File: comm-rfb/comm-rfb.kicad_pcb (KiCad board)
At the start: 4 copper layers, 90.2 x 95.9 mm, 59 parts, among them J1 PC104_Connector, J10 Radio Test Connector, J11 System Test Connector, J12 Programming Header, J2 TFM-110-02-SM-D-A-K-TR, J3 TFM-110-02-SM-D-A-K-TR, J4 TFM-110-02-SM-D-A-K-TR, J5 TFM-110-02-SM-D-A-K-TR, J6 Conn_Coaxial, J7 Conn_Coaxial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

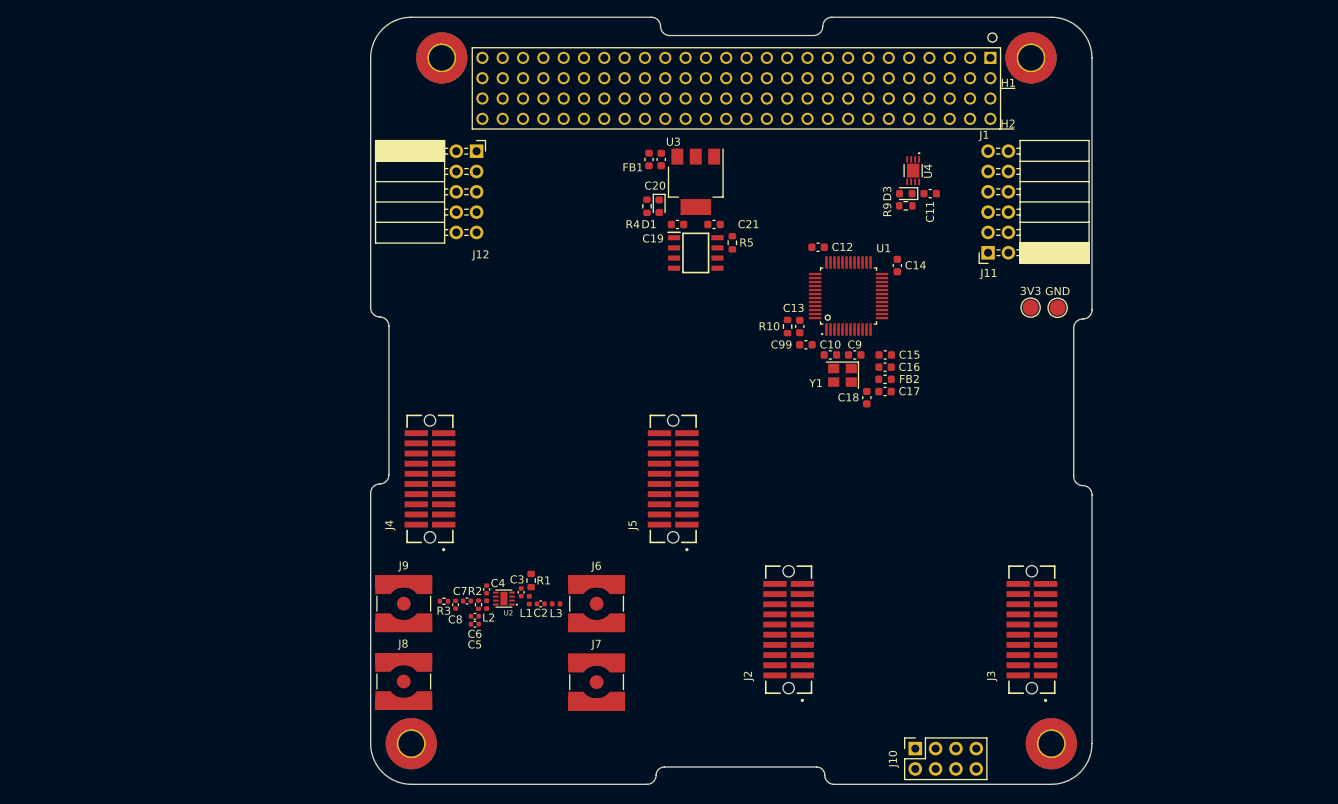
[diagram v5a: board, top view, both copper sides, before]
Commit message: comm-rfb: continue with new layout
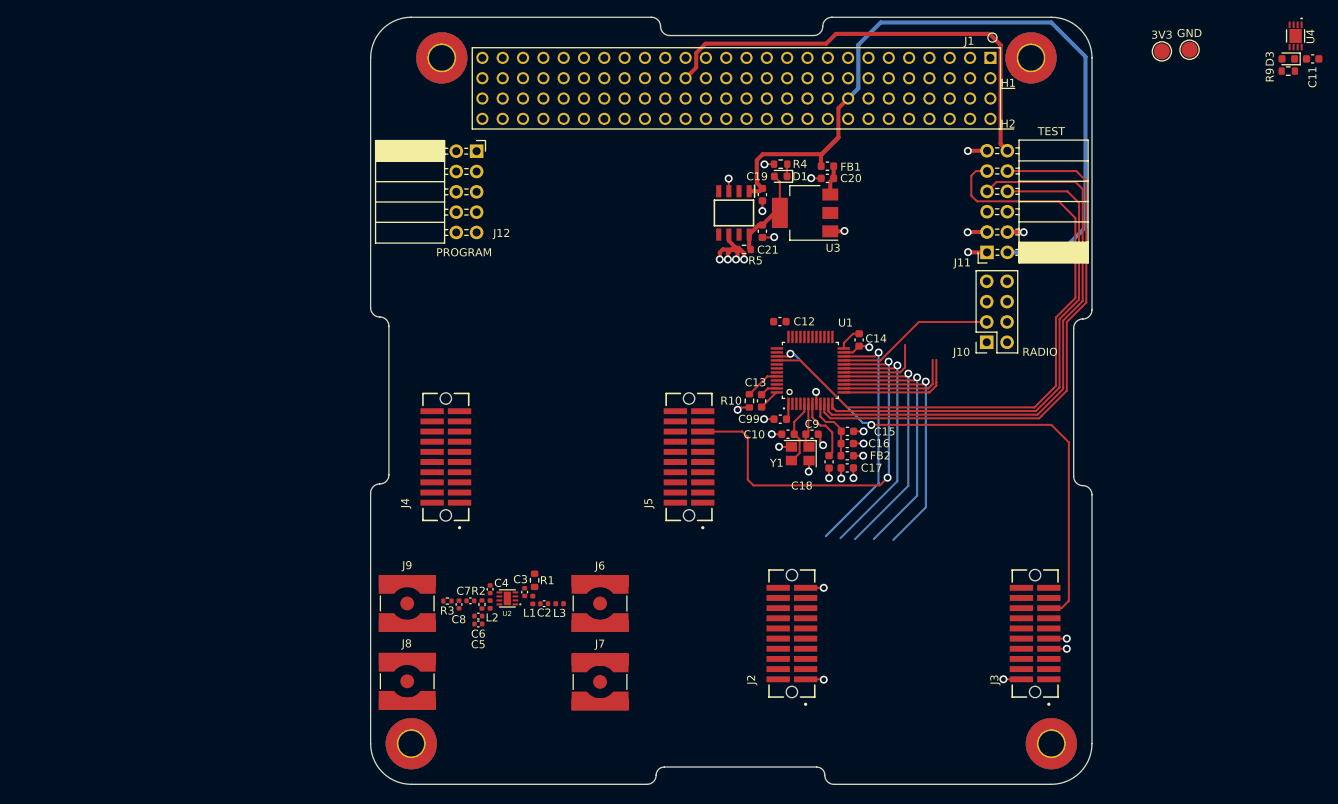
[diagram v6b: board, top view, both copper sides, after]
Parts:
- moved J10 51.6 mm to (186.2, 87.6), turned to 180 degrees
- moved C11 50.7 mm to (227.0, 52.2)
- moved D3 50.7 mm to (223.9, 52.2)
- moved R9 50.7 mm to (223.9, 53.7)
- moved U4 50.7 mm to (224.8, 49.3)
- moved TP2 36.2 mm to (211.6, 51.1)
- moved TP1 36.0 mm to (208.1, 51.3)
- moved FB1 22.3 mm to (166.3, 65.6), turned to 180 degrees
- moved C20 20.9 mm to (166.3, 67.1), turned to 180 degrees
- moved R4 17.5 mm to (160.5, 65.4), turned to 0 degrees
- moved D1 15.6 mm to (160.5, 66.9), turned to 180 degrees
- moved U3 14.2 mm to (163.5, 71.5), turned to 180 degrees
- moved C9 11.3 mm to (164.4, 99.1)
- moved C19 11.3 mm to (158.2, 69.2), turned to -90 degrees
- moved C10 11.2 mm to (161.4, 99.1)
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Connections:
- J1 pad 41: unconnected-(J1-Pad41) -> I2C2-SDA
- J1 pad 43: unconnected-(J1-Pad43) -> I2C2-SCK
- J11 pad 10: SYS-GPIO3 -> SYS-GPIO1
- J11 pad 5: I2C-SCK -> I2C2-SCK
- J11 pad 6: I2C-SDA -> I2C2-SDA
- J11 pad 8: SYS-GPIO1 -> SYS-GPIO3
- U1 pad 32: I2C2-SCLK -> I2C2-SCK
- U1 pad 45: I2C-SCK -> I2C1-SCK
- U1 pad 46: I2C-SDA -> I2C1-SDA
- U4 pad 2: I2C2-SCLK -> I2C2-SCK
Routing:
- net SW6-5V: track 0.00 -> 97.8 mm
- net SYS-GPIO4: track 0.00 -> 79.3 mm
- net SYS-GPIO1: track 0.00 -> 70.7 mm
- net SYS-GPIO2: track 0.00 -> 70.6 mm
- net RESET-RX: track 0.00 -> 63.9 mm, vias 0 -> 2
- net SYS-GPIO3: track 0.00 -> 63.9 mm
- net 5V0-CHG: track 0.00 -> 56.9 mm
- net RESET-TX: track 0.00 -> 49.7 mm, vias 0 -> 2
- net GND: track 0.36 -> 41.2 mm, vias 0 -> 23
- net SPI1-SCLK: track 0.00 -> 31.9 mm, vias 0 -> 1
- net SPI1-MISO: track 0.00 -> 31.8 mm, vias 0 -> 1
- net SPI1-MOSI: track 0.00 -> 31.6 mm, vias 0 -> 1
- net SPI1-CSN-RX: track 0.00 -> 31.4 mm, vias 0 -> 1
- net AMP-ENABLE: track 0.00 -> 30.3 mm, vias 0 -> 1
- net +3V3: track 0.00 -> 28.0 mm, vias 0 -> 9
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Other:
- board text added: "PROGRAM"
- board text added: "RADIO"
- board text added: "TEST"

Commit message: comm-rfb: finish connections from MCU
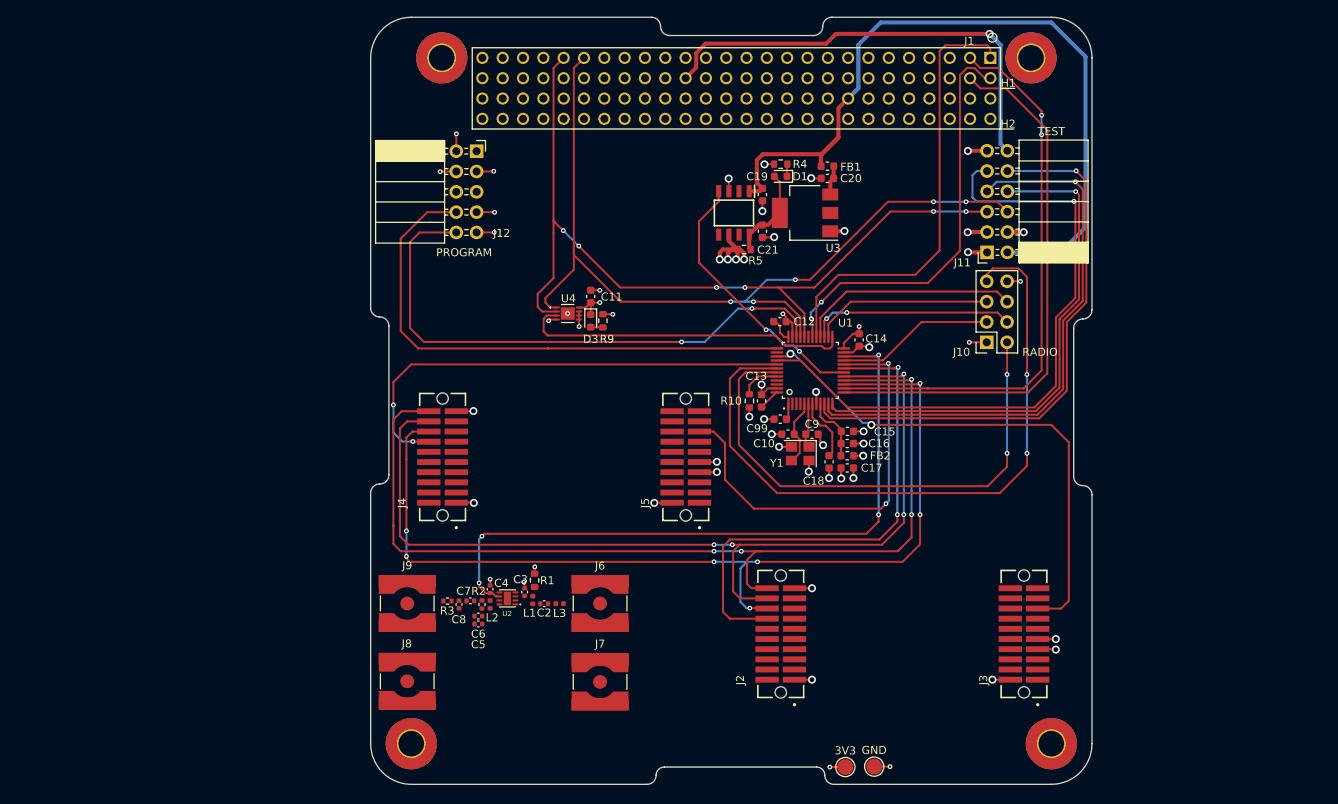
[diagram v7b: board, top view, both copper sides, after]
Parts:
- moved TP2 97.9 mm to (172.2, 140.7)
- moved TP1 97.8 mm to (168.6, 140.7)
- moved U4 97.4 mm to (133.9, 84.0), turned to 0 degrees
- moved C11 95.0 mm to (136.7, 81.9), turned to 90 degrees
- moved D3 93.1 mm to (136.7, 84.9), turned to -90 degrees
- moved R9 91.2 mm to (138.3, 84.9), turned to 90 degrees
- moved J2 1.39 mm to (160.5, 124.1)
- moved J3 1.39 mm to (190.9, 124.1)
- moved J5 0.41 mm to (148.6, 102.0)
- moved J4 0.41 mm to (118.2, 102.0)
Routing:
- net I2C2-SDA: track 0.00 -> 108.0 mm, vias 0 -> 5
- net I2C2-SCK: track 0.00 -> 104.2 mm, vias 0 -> 6
- net SPI1-MISO: track 31.8 -> 123.1 mm, vias 1 -> 4
- net SPI1-SCLK: track 31.9 -> 122.1 mm, vias 1 -> 7
- net SPI1-MOSI: track 31.6 -> 119.0 mm, vias 1 -> 4
- net SPI2-CSN: track 0.00 -> 86.1 mm, vias 0 -> 2
- net SWDIO: track 0.00 -> 70.5 mm, vias 0 -> 2
- net SWCLK: track 0.00 -> 67.8 mm
- net SPI2-CE: track 0.00 -> 65.6 mm, vias 0 -> 2
- net SPI1-CSN-TX: track 0.00 -> 60.1 mm, vias 0 -> 2
- net COMM-TXD: track 0.00 -> 55.7 mm
- net COMM-CTS: track 14.4 -> 69.8 mm, vias 0 -> 2
- net AMP-ENABLE: track 30.3 -> 85.1 mm, vias 1 -> 4
- net COMM-RTS: track 15.1 -> 69.2 mm
- net COMM-RXD: track 0.00 -> 51.6 mm, vias 0 -> 2
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
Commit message: comm-rfb: finish RF front end
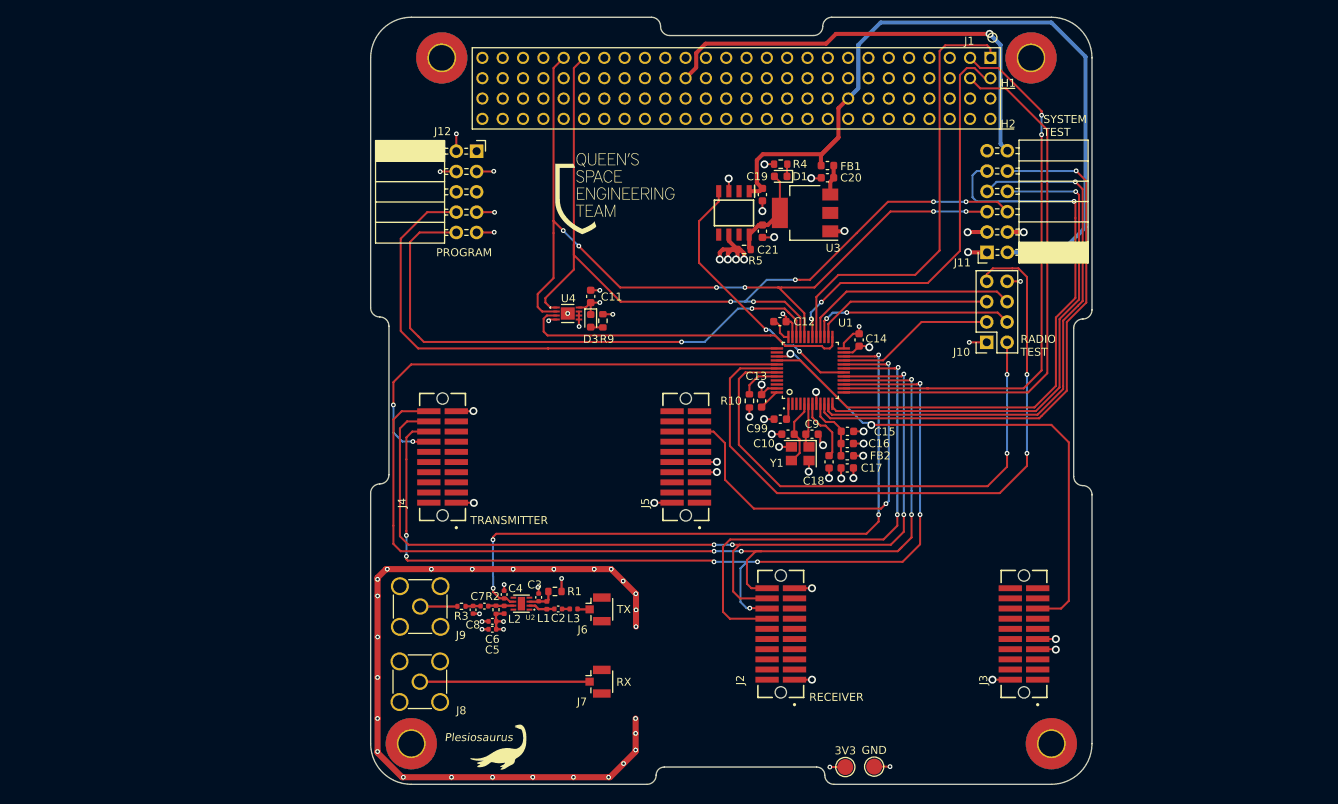
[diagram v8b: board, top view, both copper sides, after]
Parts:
- added G***: LOGO, LOGO, F.Cu at (139.8, 68.9)
- added G***: LOGO, LOGO, F.Cu at (125.2, 138.2)
- J6, J7: footprint Connector_Coaxial:SMA_Amphenol_132134-10_Vertical -> Connector_Coaxial:U.FL_Hirose_U.FL-R-SMT-1_Vertical
- J8, J9: footprint Connector_Coaxial:SMA_Amphenol_132134-10_Vertical -> Connector_Coaxial:SMA_Amphenol_132134-11_Vertical
- moved R1 2.90 mm to (132.3, 118.8), turned to 180 degrees
- moved L1 1.87 mm to (131.2, 120.5)
- moved L3 1.87 mm to (134.6, 121.0)
- moved C8 1.87 mm to (122.0, 121.1)
- moved R3 1.87 mm to (120.6, 120.6)
- moved C4 1.87 mm to (125.9, 119.2)
- moved C5 1.87 mm to (124.4, 123.5)
- moved C6 1.87 mm to (124.4, 122.5)
- moved C7 1.87 mm to (123.4, 120.6)
- moved L2 1.87 mm to (125.9, 121.1)
- moved R2 1.87 mm to (124.9, 121.1)
- moved U2 1.87 mm to (128.1, 120.3)
- moved C2 1.87 mm to (132.7, 121.0)
- moved C3 1.87 mm to (130.2, 119.5)
- moved J9 1.67 mm to (115.4, 120.7)
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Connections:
- J11 pad 11: GND-CHG -> GND
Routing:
- net GND: track 69.7 -> 177.6 mm, vias 40 -> 70
- net /RF Front End (Tx & Rx)/RX-TO-EM: track 0.00 -> 21.2 mm
- net +3V3: track 49.5 -> 55.1 mm, vias 18 -> 20
- net /RF Front End (Tx & Rx)/AMP-TO-EXT: track 0.00 -> 4.66 mm
- net Net-(C3-Pad1): track 0.00 -> 3.53 mm
- net Net-(C2-Pad2): track 0.00 -> 3.31 mm
- net Net-(C7-Pad1): track 0.00 -> 3.18 mm
- net GND-CHG: track 2.41 -> 0.00 mm, vias 1 -> 0
- net Net-(C7-Pad2): track 0.00 -> 1.91 mm
- net /RF Front End (Tx & Rx)/EM-TO-AMP: track 0.00 -> 1.53 mm
- net Net-(C2-Pad1): track 0.00 -> 0.97 mm
- net AMP-ENABLE: track 85.1 -> 84.2 mm
- net XOSC_OUT: track 6.50 -> 5.68 mm
- net SPI1-MOSI: track 119.0 -> 119.7 mm
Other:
- board text added: "Plesiosaurus"
- board text added: "RADIO TEST"
- board text added: "RECEIVER"
- board text added: "RX"
- board text added: "SYSTEM TEST"
- board text added: "TRANSMITTER"
- board text added: "TX"
- board text removed: "RADIO"
- board text removed: "TEST"
